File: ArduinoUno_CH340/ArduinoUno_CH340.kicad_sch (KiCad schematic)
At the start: 58 parts, among them J1 Jack_DC, J10 I2C, J11 Servo, J2 USB_B, J3 Header_4P, J4 ICSPx, J5 POWER, J6 IOH, J7 ANALOG, J8 IOL, J9 RxTx, Q1 MOS-P_FDN304P, SW1 SW_Push_NO, U1 MC33269-SOT, U2 CH340G, U3 LM358D, U4 ATmega328-P, U5 LP2985-3.3, Y1 16MHz, Y2 16MHz

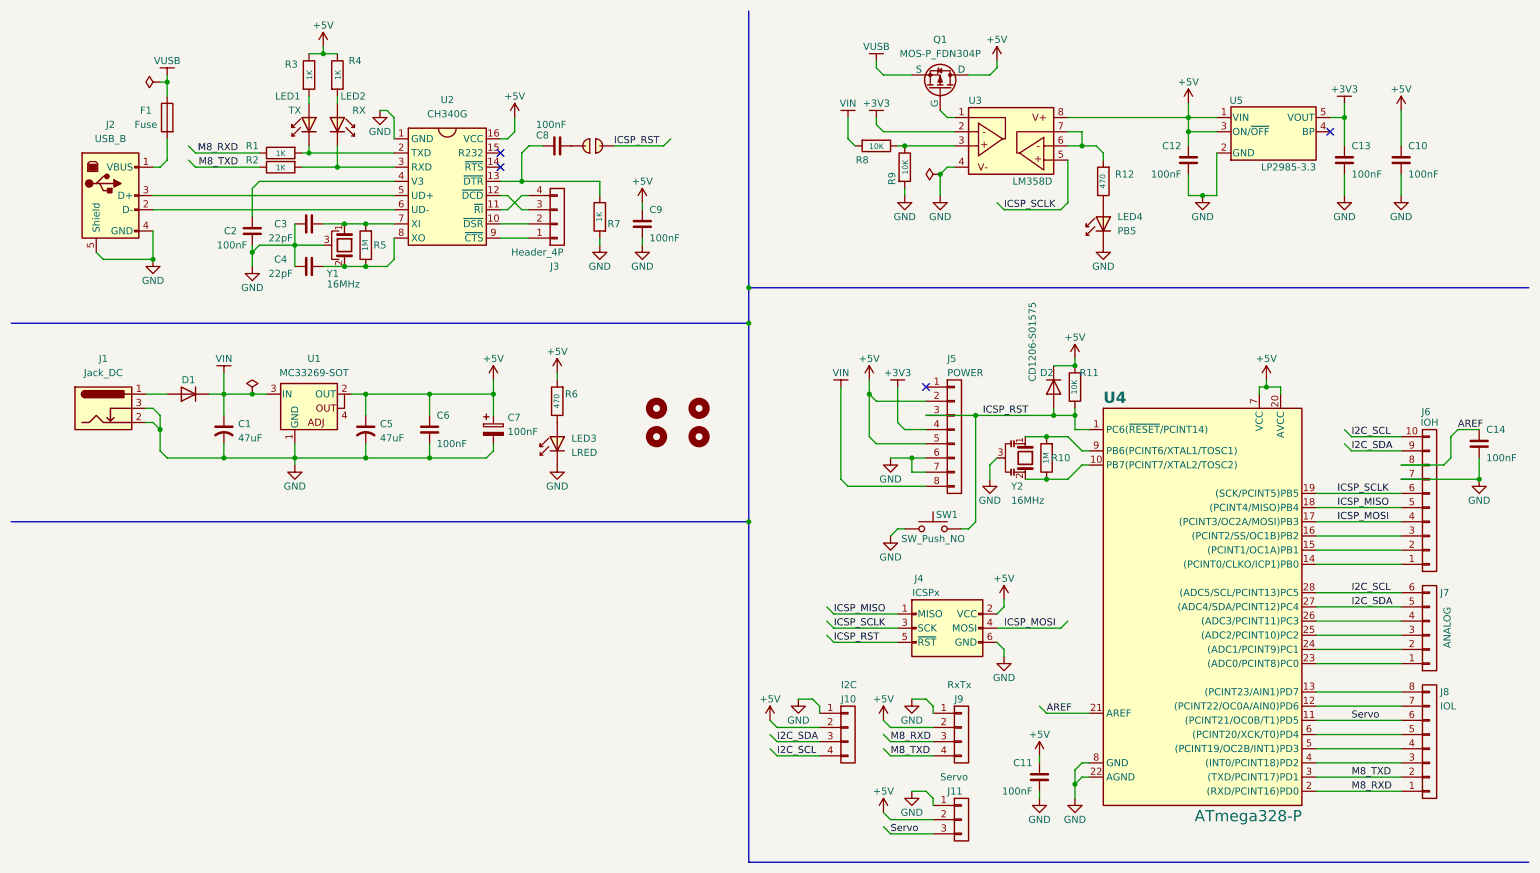
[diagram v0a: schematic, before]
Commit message: Complete Arduino Uno CH340
Complete Project Arduino uno CH340
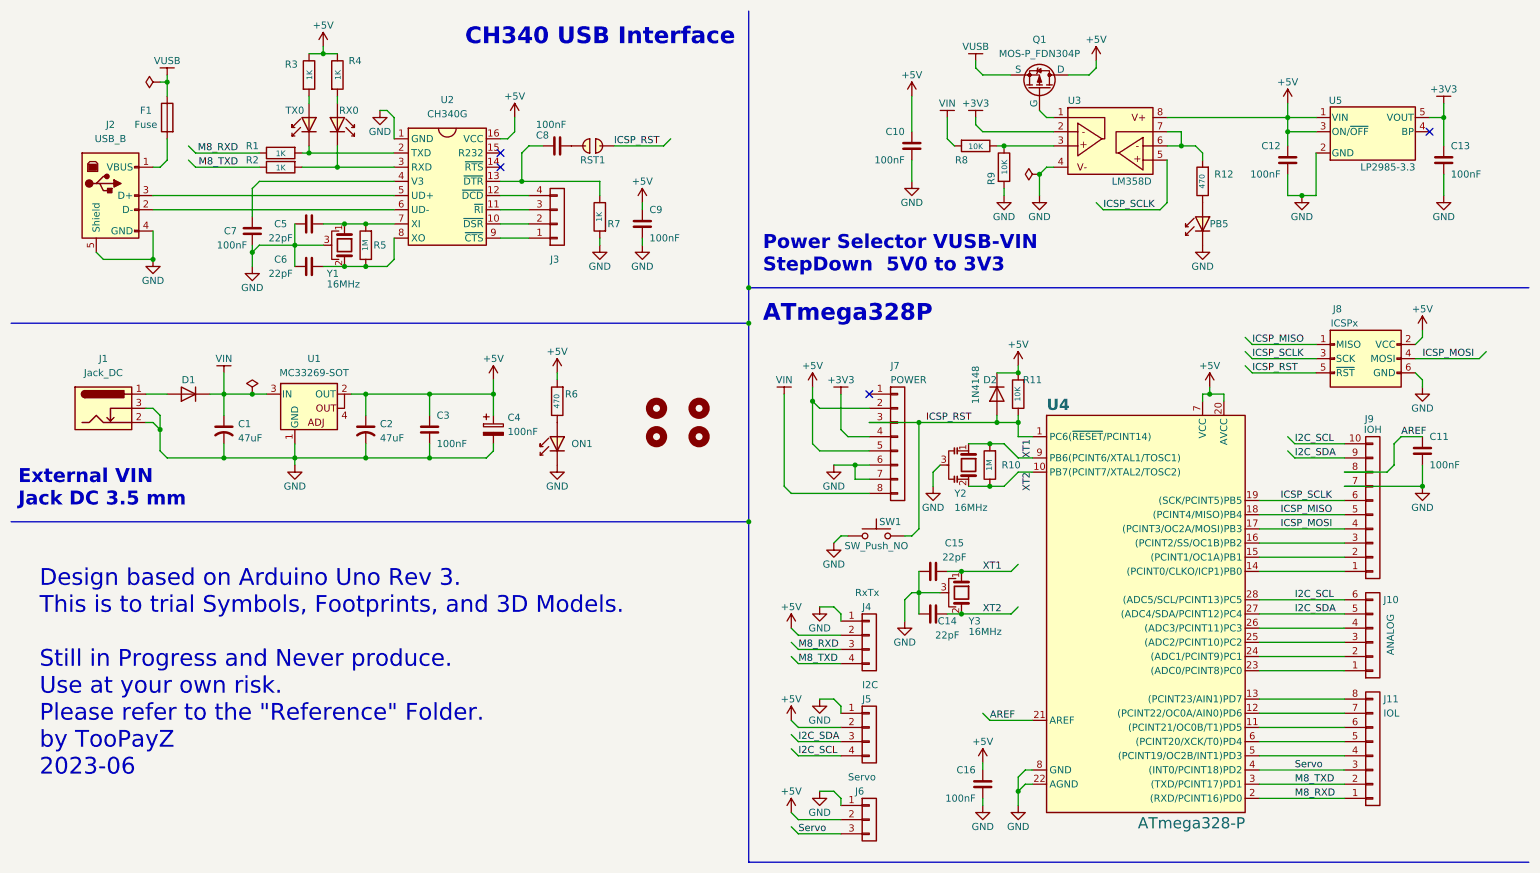
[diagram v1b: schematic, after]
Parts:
- added C14, C15: 22pF, 02pyzPassive:C_0805_HandSolder, symbol 02pyzPassive:C
- added Y3: 16MHz, 02pyzPassive:Crystal_HC49-4H_Vertical_GND, symbol 02pyzPassive:Crystal_GND
- C1: footprint 02pyzPassive:C_Radial_D4.0mm_H5.0mm_P1.50mm -> 02pyzPassive:C_Radial_D6.3mm_P2.50mm
- C2: renamed from C5; footprint 02pyzPassive:C_Radial_D4.0mm_H5.0mm_P1.50mm -> 02pyzPassive:C_Radial_D6.3mm_P2.50mm
- D2: value CD1206-S01575 -> 1N4148; footprint 03pyzActive:D_1206_HandSolder -> 03pyzActive:D_SOD-123
- ON1: renamed from LED3; footprint 03pyzActive:D_0805_HandSolder -> 03pyzActive:LED_0805_HandSolder
- PB5: renamed from LED4; footprint 03pyzActive:LED_D3.0mm -> 03pyzActive:LED_0805_HandSolder
- RX0: renamed from LED2; footprint 03pyzActive:LED_D3.0mm -> 03pyzActive:LED_0805_HandSolder
- TX0: renamed from LED1; footprint 03pyzActive:LED_D3.0mm -> 03pyzActive:LED_0805_HandSolder
- renumbered C14 to C11, C11 to C16, C6 to C3, C7 to C4, C3 to C5, C4 to C6, C2 to C7, J7 to J10, J8 to J11, J9 to J4, J10 to J5, J11 to J6, J5 to J7, J4 to J8, J6 to J9, SOL1 to RST1
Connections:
- net GND: now also C14.1, C15.1, Y3.3
- net Servo: now also J11.3 (Pin_3), U4.4 ((INT0/PCINT18)PD2); no longer J11.6 (Pin_6), U4.11 ((PCINT21/OC0B/T1)PD5)
- net at J3.3 (Pin_3): now also U2.11 (~{RI}); no longer U2.12 (~{DCD})
- net at J3.4 (Pin_4): now also U2.12 (~{DCD}); no longer U2.11 (~{RI})
- net XT1: now reaches R10.1, U4.9 (PB6(PCINT6/XTAL1/TOSC1)), Y2.1
- net XT1: now also C15.2, Y3.1
- net XT2: now reaches R10.2, U4.10 (PB7(PCINT7/XTAL2/TOSC2)), Y2.2
- net XT2: now also C14.2, Y3.2
- new net: J11.6 (Pin_6), U4.11 ((PCINT21/OC0B/T1)PD5)
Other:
- note added: "ATmega328P"
- note added: "CH340 USB Interface"
- note added: "Design based on Arduino Uno Rev 3. This is to trial Symbols, Footprints, and 3D Models. Still in Progress and Never produce. Use at your own risk. Please refer to the "Reference" Folder. by TooPayZ 2023-06"
- note added: "External VIN Jack DC 3.5 mm"
- note added: "Power Selector VUSB-VIN StepDown 5V0 to 3V3"
- company: (none) -> TooPayz
- title: (none) -> KiCAD trial Symbol, Footprint, and 3D Models
- moved on the sheet: C10, C11, C12, C13, C16, D2, J10, J11, J4, J5, J6, J7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
